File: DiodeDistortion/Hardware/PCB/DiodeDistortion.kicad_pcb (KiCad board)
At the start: 2 copper layers, 20 x 100 mm, 22 parts, among them J1 THONKICONN, J2 THONKICONN, J3 THONKICONN, J4 Conn_01x10_Pin, U1 TL074, U3 NSL-32

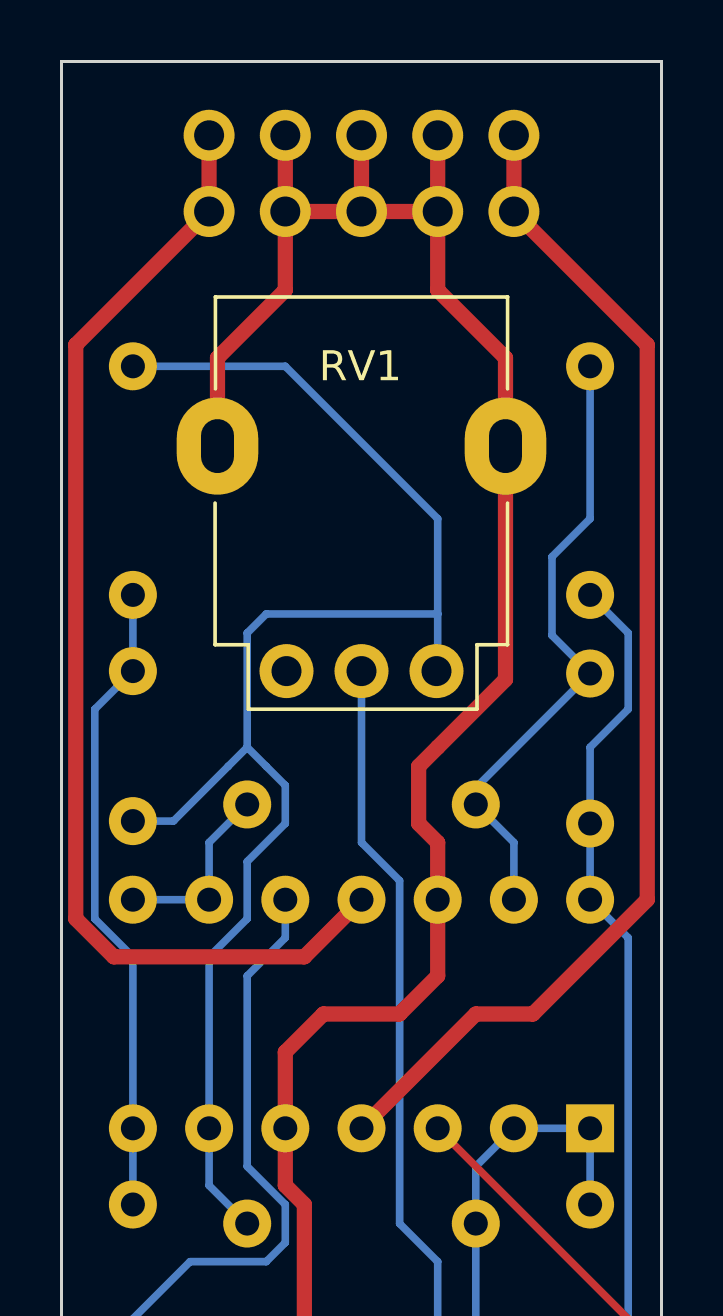
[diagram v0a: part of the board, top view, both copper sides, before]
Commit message: Added power filtering to diode distortion
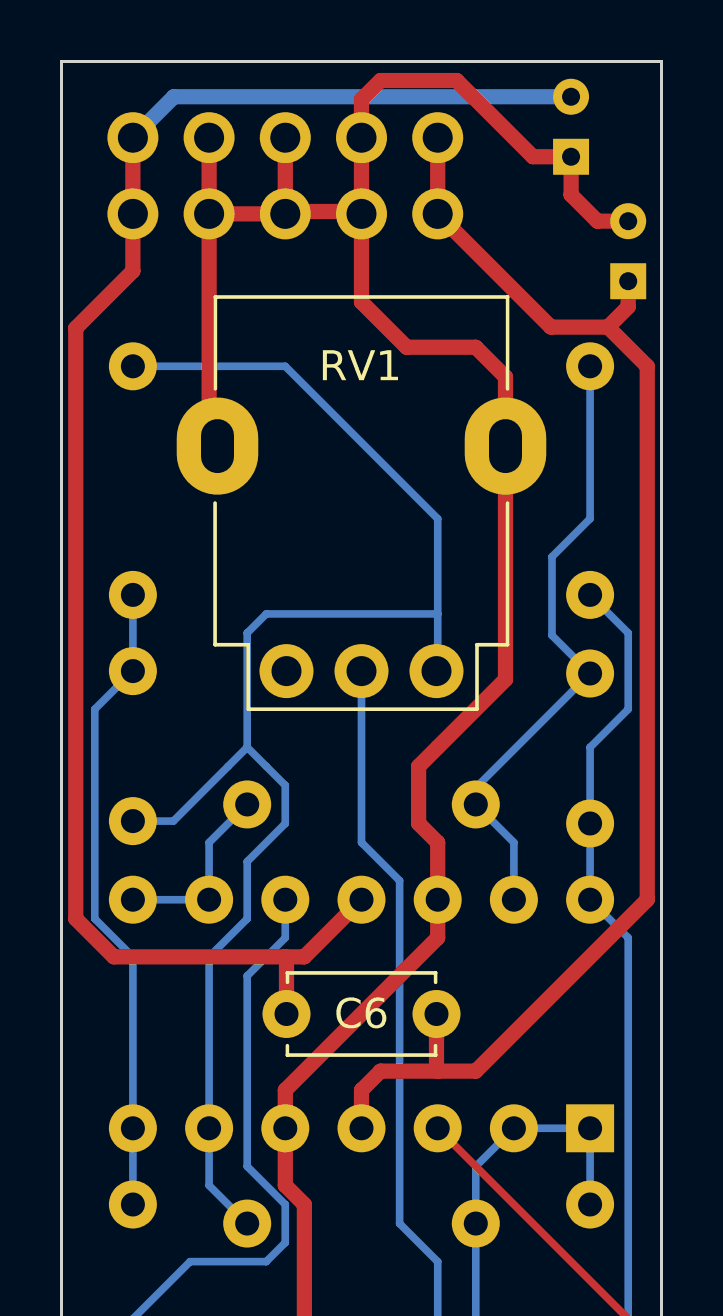
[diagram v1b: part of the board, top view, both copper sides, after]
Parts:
- added C4: 10uF, Capacitor_THT:CP_Radial_D4.0mm_P2.00mm, B.Cu at (42.5, 28.6)
- added C5: 10uF, Capacitor_THT:CP_Radial_D4.0mm_P2.00mm, B.Cu at (44.5, 32.7)
- added C6: 100nF, Capacitor_THT:C_Disc_D4.7mm_W2.5mm_P5.00mm, F.Cu at (38.1, 57.1)
- R1: value 1M -> 100k
- R9: value 330 -> 1k
- moved J4 2.54 mm to (38.1, 27.9)
- renumbered U3 to U2
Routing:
- net -12V: track 38.8 -> 54.8 mm
- net GND: track 153.8 -> 166.8 mm
- net +12V: track 40.0 -> 46.6 mm
